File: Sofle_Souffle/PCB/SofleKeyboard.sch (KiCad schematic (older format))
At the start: 84 parts, among them J2 4PIN, J3 OLED, P1 i2c_pin, P2 i2c_pin, SW1 SW_PUSH-MX_W_LED, SW10 SW_PUSH-MX_W_LED, SW11 SW_PUSH-MX_W_LED, SW12 SW_PUSH-MX_W_LED, SW13 SW_PUSH-MX_W_LED, SW14 SW_PUSH-MX_W_LED, SW15 SW_PUSH-MX_W_LED, SW16 SW_PUSH-MX_W_LED, SW17 SW_PUSH-MX_W_LED, SW18 SW_PUSH-MX_W_LED, SW19 SW_PUSH-MX_W_LED, SW2 SW_PUSH-MX_W_LED, SW20 SW_PUSH-MX_W_LED, SW21 SW_PUSH-MX_W_LED, SW22 SW_PUSH-MX_W_LED, SW23 SW_PUSH-MX_W_LED, SW24 SW_PUSH-MX_W_LED, SW25 Rotary_Encoder_Switch, SW26 SW_PUSH-MX_W_LED, SW27 SW_PUSH-MX_W_LED, SW28 SW_PUSH-MX_W_LED, SW29 SW_PUSH-MX_W_LED, SW3 SW_PUSH-MX_W_LED, SW30 SW_PUSH-MX_W_LED, SW4 SW_PUSH-MX_W_LED, SW5 SW_PUSH-MX_W_LED, SW6 SW_PUSH-MX_W_LED, SW7 SW_PUSH-MX_W_LED, SW8 SW_PUSH-MX_W_LED, SW9 SW_PUSH-MX_W_LED, U1 ProMicro

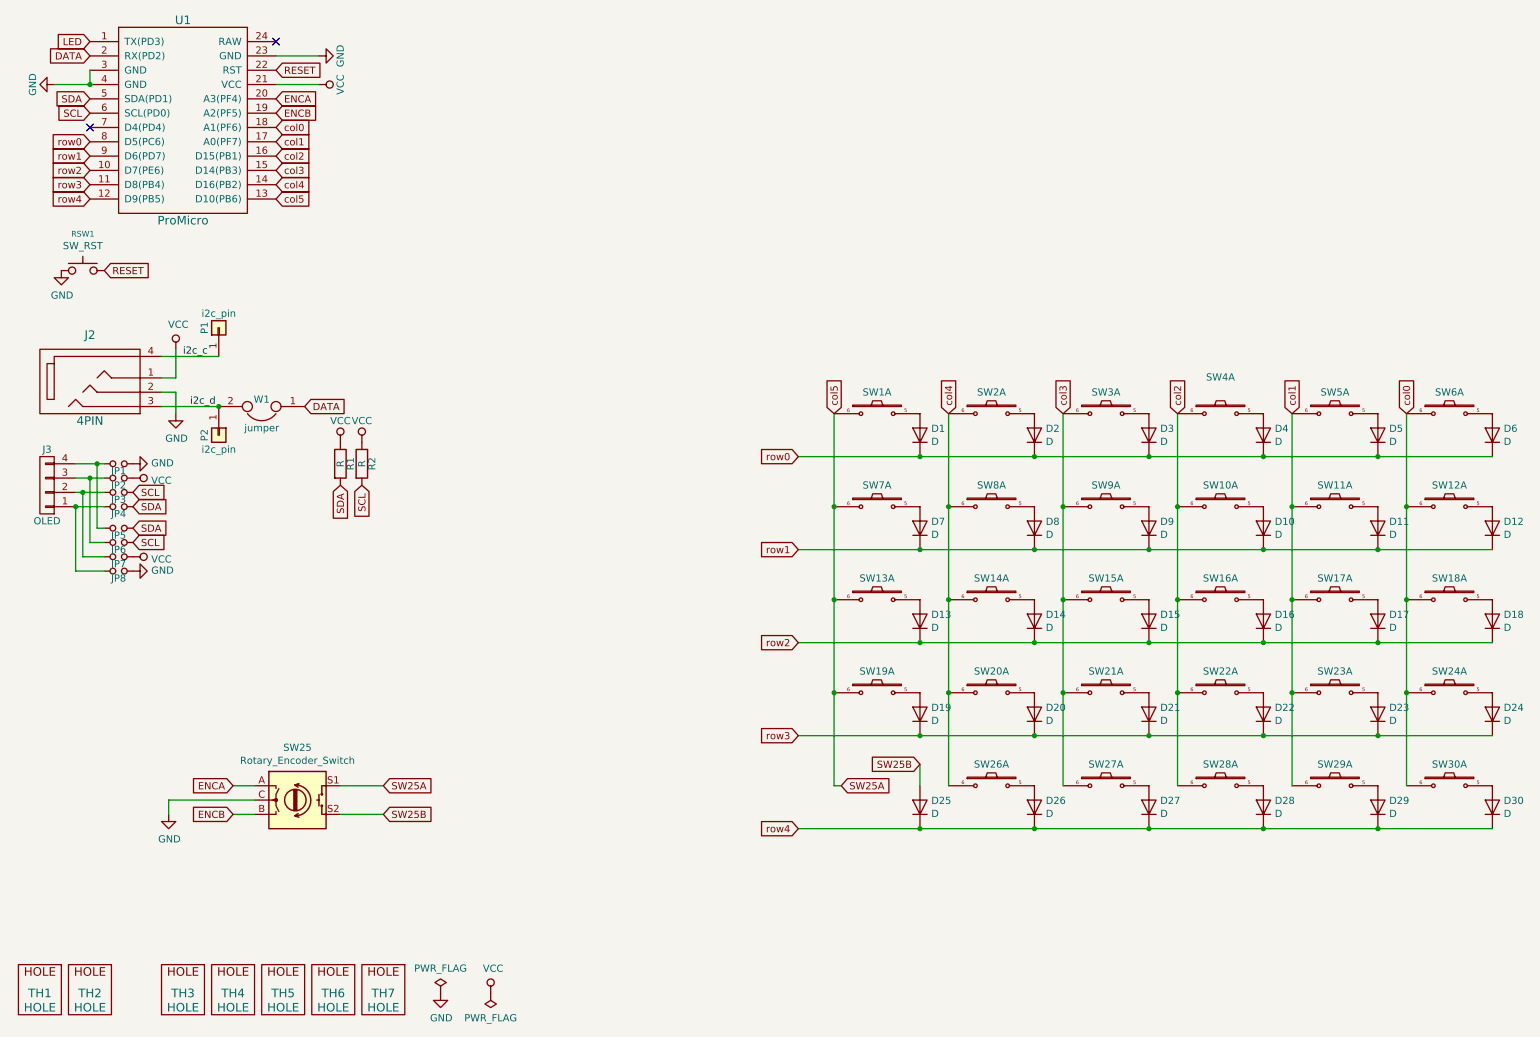
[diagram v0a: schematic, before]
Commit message: Completed Soufflé board with palm key. Missing the roller encoder.
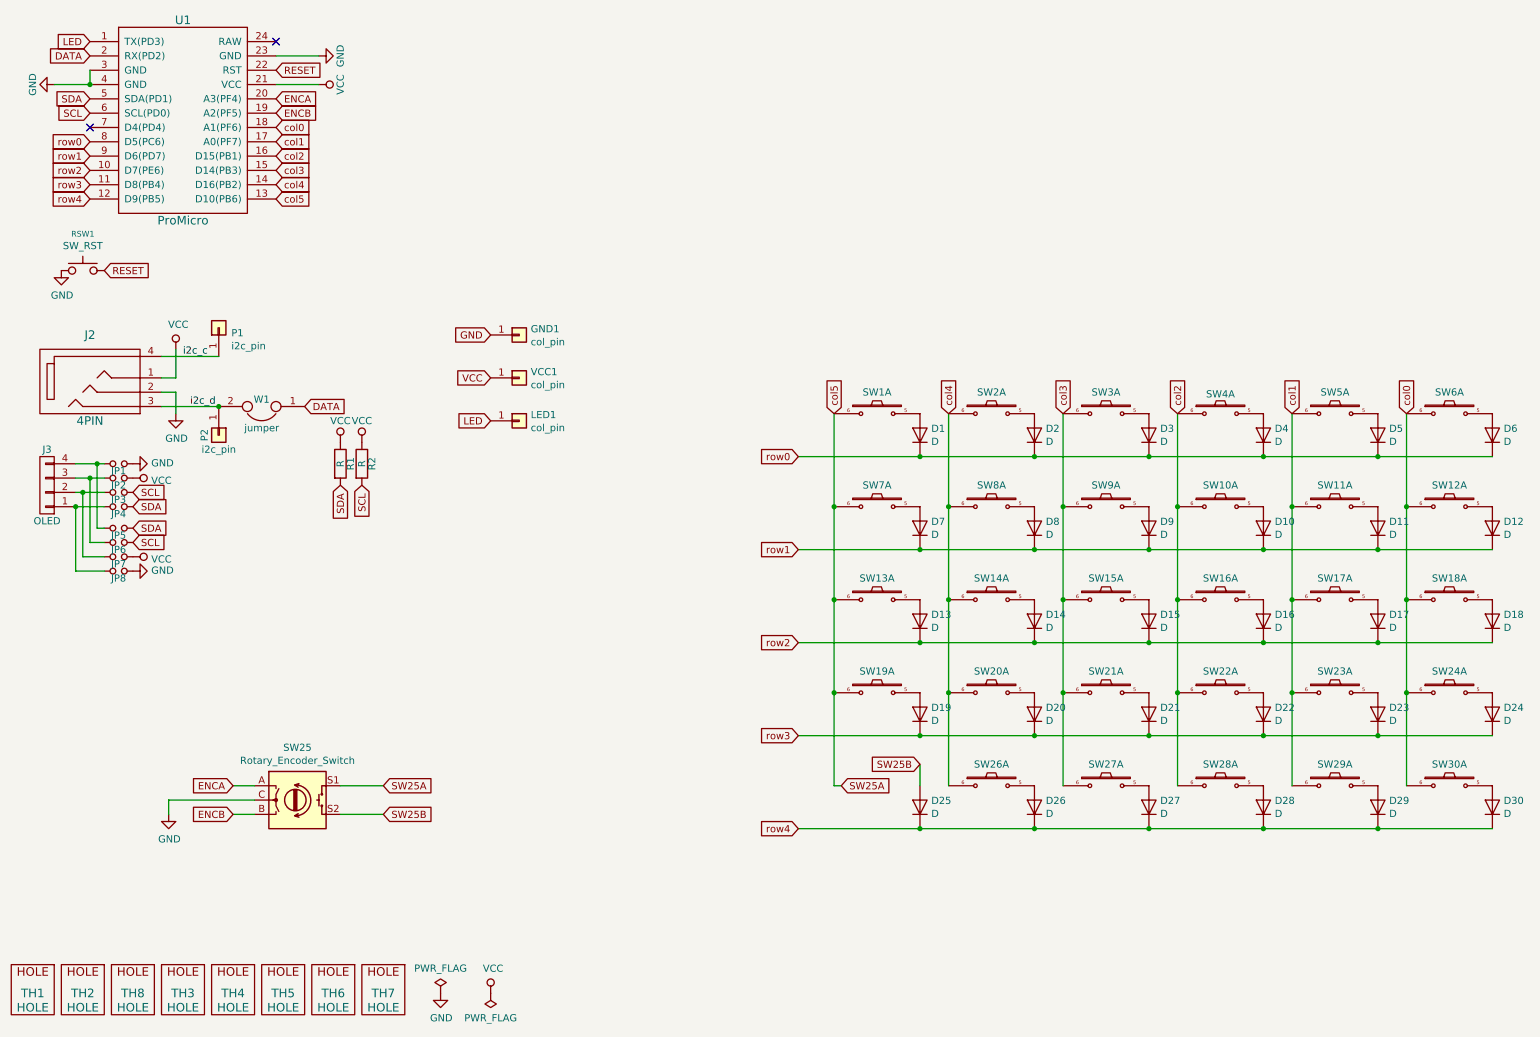
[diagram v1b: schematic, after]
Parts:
- added GND1, LED1, VCC1: col_pin, SofleRGB:1pin_conn, symbol SofleKeyboard-rescue:i2c_pin-Lily58-cache
- added TH8: HOLE, SofleRGB:M2_HOLE_PCB, symbol SofleKeyboard-rescue:HOLE-Lily58-cache-Lily58_Pro-rescue
- D30: footprint SofleRGB:Jumper -> SofleRGB:crkbd-diode
- J2: footprint SofleRGB:Jumper -> SofleRGB:MJ-4PP-9
- J3: footprint SofleRGB:Jumper -> SofleRGB:OLED_4Pin
- SW1, SW10, SW11, SW12, SW13, SW14, SW15, SW16, SW17, SW18, SW19, SW2, SW20, SW21, SW22, SW23, SW24, SW26, SW27, SW28, SW29, SW3, SW30, SW4, SW5, SW6, SW7, SW8, SW9: footprint SofleRGB:SK6812MINI_and_cherry -> SofleRGB:SK6812MINI_and_cherry_NoLEDPads
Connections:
- net GND: now also GND1.1 (Pin_1)
- net LED: now also LED1.1 (Pin_1)
- net VCC: now also VCC1.1 (Pin_1)
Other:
- moved on the sheet: TH1, TH2

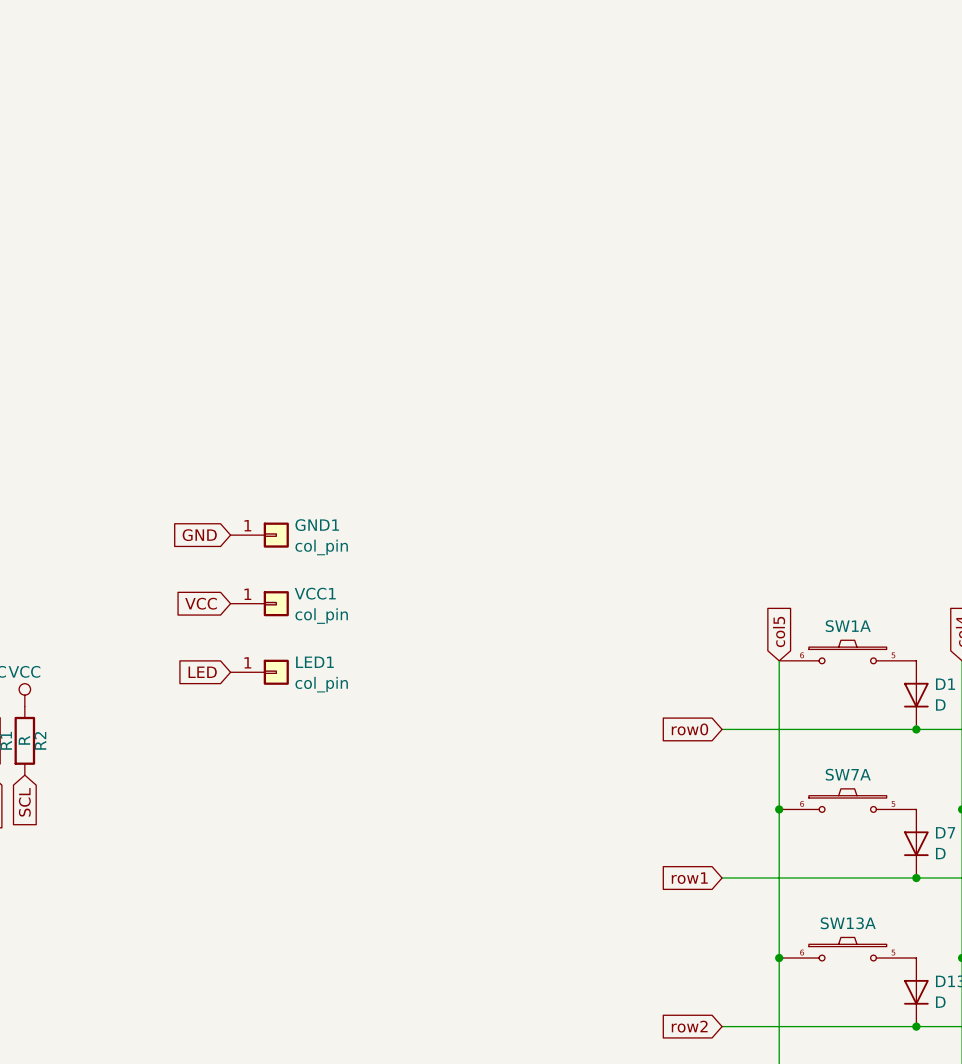
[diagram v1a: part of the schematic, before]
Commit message: Added EVQWGD001 and 5pin to schematic, and 5pin to PCB.
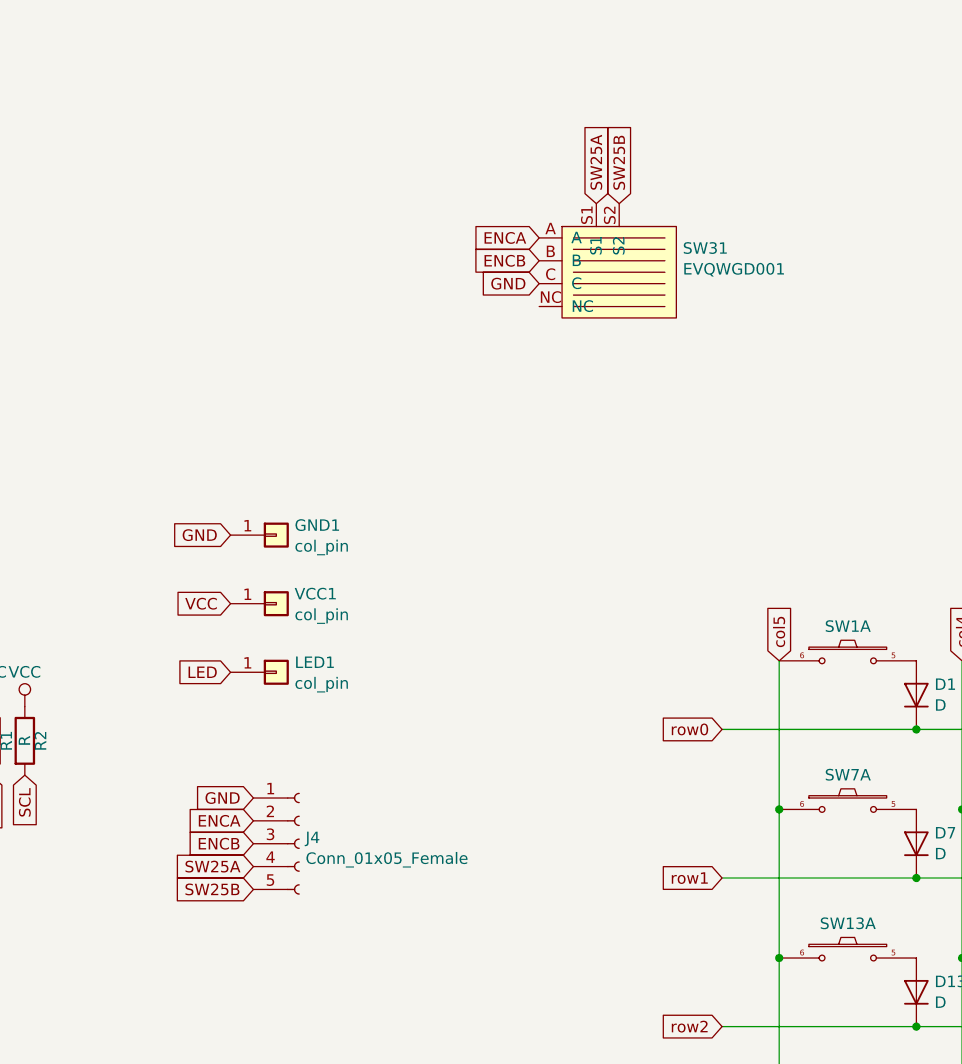
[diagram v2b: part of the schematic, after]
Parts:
- added J4: Conn_01x05_Female, Connector_PinHeader_2.54mm:PinHeader_1x05_P2.54mm_Horizontal, symbol Connector:Conn_01x05_Female
- added SW31: EVQWGD001, SofleRGB:EVQWGD001, symbol evqwgd001:EVQWGD001
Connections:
- net ENCA: now also J4.2 (Pin_2), SW31.A
- net ENCB: now also J4.3 (Pin_3), SW31.B
- net GND: now also J4.1 (Pin_1), SW31.C
- net SW25A: now also J4.4 (Pin_4), SW31.S1
- net SW25B: now also J4.5 (Pin_5), SW31.S2
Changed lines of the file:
@@
 Text GLabel 3900 3500 0    50   Input ~ 0
 LED
+$Comp
+L evqwgd001:EVQWGD001 SW31
+U 1 1 61C5400C
+P 5600 1700
+F 0 "SW31" H 5878 1754 50  0000 L CNN
+F 1 "EVQWGD001" H 5878 1663 50  0000 L CNN
+F 2 "SofleRGB:EVQWGD001" H 5600 1700 50  0001 C CNN
+F 3 "" H 5600 1700 50  0001 C CNN
+	1    5600 1700
+	1    0    0    -1
+$EndComp
+Text GLabel 5250 1600 0    50   Input ~ 0
+ENCA
+Text GLabel 5250 1700 0    50   Input ~ 0
+ENCB
+Text GLabel 5250 1800 0    50   Input ~ 0
+GND
+Text GLabel 5500 1450 1    50   Input ~ 0
+SW25A
+Text GLabel 5600 1450 1    50   Input ~ 0
+SW25B
+$Comp
+L Connector:Conn_01x05_Female J4
+U 1 1 61C6FCA3
+P 4200 4250
+F 0 "J4" H 4228 4276 50  0000 L CNN
+F 1 "Conn_01x05_Female" H 4228 4185 50  0000 L CNN
+F 2 "Connector_PinHeader_2.54mm:PinHeader_1x05_P2.54mm_Horizontal" H 4200 4250 50  0001 C CNN
+F 3 "~" H 4200 4250 50  0001 C CNN
+	1    4200 4250
+	1    0    0    -1
+$EndComp
+Text GLabel 4000 4050 0    50   Input ~ 0
+GND
+Text GLabel 4000 4150 0    50   Input ~ 0
+ENCA
+Text GLabel 4000 4250 0    50   Input ~ 0
+ENCB
+Text GLabel 4000 4350 0    50   Input ~ 0
+SW25A
+Text GLabel 4000 4450 0    50   Input ~ 0
+SW25B
 $EndSCHEMATC

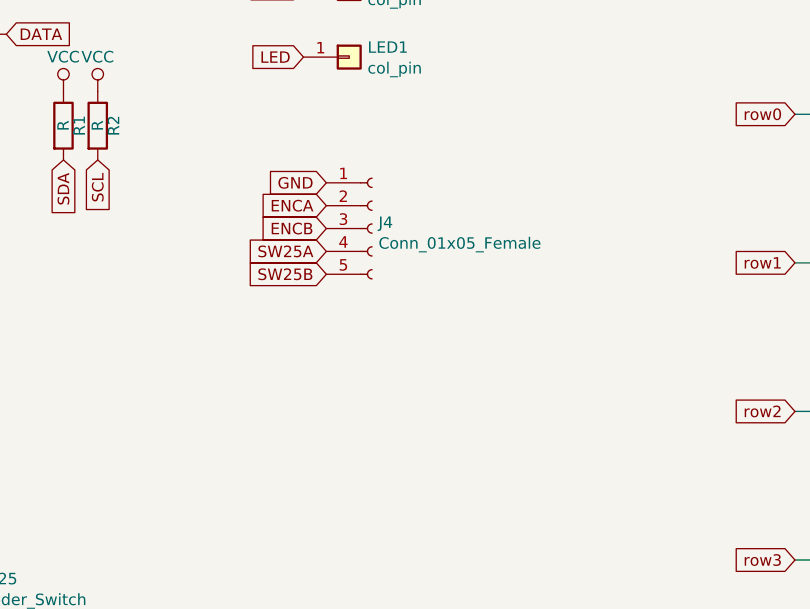
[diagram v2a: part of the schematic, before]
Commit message: Removed 5pin connector on the right side of the case/pcb.
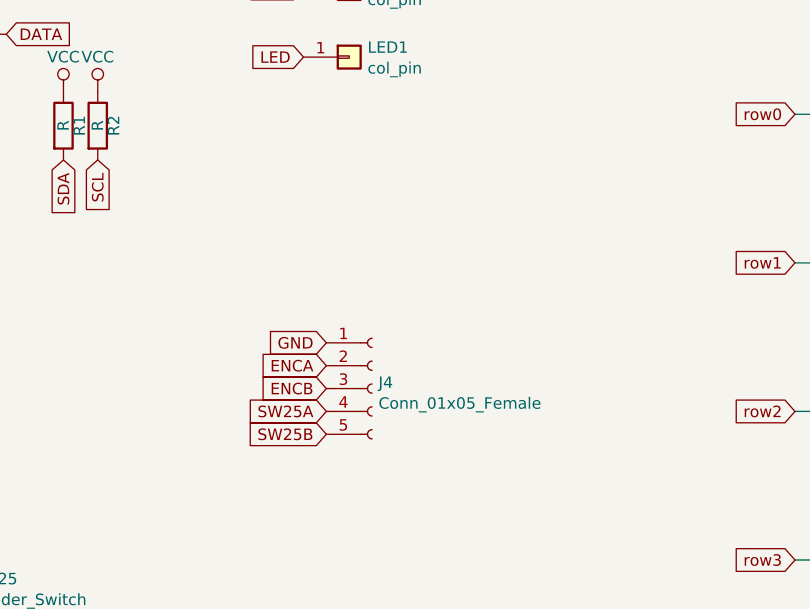
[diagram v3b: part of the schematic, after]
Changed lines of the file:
@@
 $Comp
 L Connector:Conn_01x05_Female J4
-U 1 1 61C6FCA3
-P 4200 4250
-F 0 "J4" H 4228 4276 50  0000 L CNN
-F 1 "Conn_01x05_Female" H 4228 4185 50  0000 L CNN
-F 2 "Connector_PinHeader_2.54mm:PinHeader_1x05_P2.54mm_Horizontal" H 4200 4250 50  0001 C CNN
-F 3 "~" H 4200 4250 50  0001 C CNN
-	1    4200 4250
+U 1 1 61C63EF0
+P 4200 4950
+F 0 "J4" H 4228 4976 50  0000 L CNN
+F 1 "Conn_01x05_Female" H 4228 4885 50  0000 L CNN
+F 2 "Connector_PinHeader_2.54mm:PinHeader_1x05_P2.54mm_Horizontal" H 4200 4950 50  0001 C CNN
+F 3 "~" H 4200 4950 50  0001 C CNN
+	1    4200 4950
 	1    0    0    -1
 $EndComp
-Text GLabel 4000 4050 0    50   Input ~ 0
+Text GLabel 4000 4750 0    50   Input ~ 0
 GND
-Text GLabel 4000 4150 0    50   Input ~ 0
+Text GLabel 4000 4850 0    50   Input ~ 0
 ENCA
-Text GLabel 4000 4250 0    50   Input ~ 0
+Text GLabel 4000 4950 0    50   Input ~ 0
 ENCB
-Text GLabel 4000 4350 0    50   Input ~ 0
+Text GLabel 4000 5050 0    50   Input ~ 0
 SW25A
-Text GLabel 4000 4450 0    50   Input ~ 0
+Text GLabel 4000 5150 0    50   Input ~ 0
 SW25B
 $EndSCHEMATC
